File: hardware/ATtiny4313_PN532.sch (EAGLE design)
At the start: 22 parts, among them IC1 ATtiny4313, J2 AVR ISP, Q1 14.7456MHz, U1 PCA9543AD,118, U3 LTC490CN8PBF, U4 LTC490CN8PBF

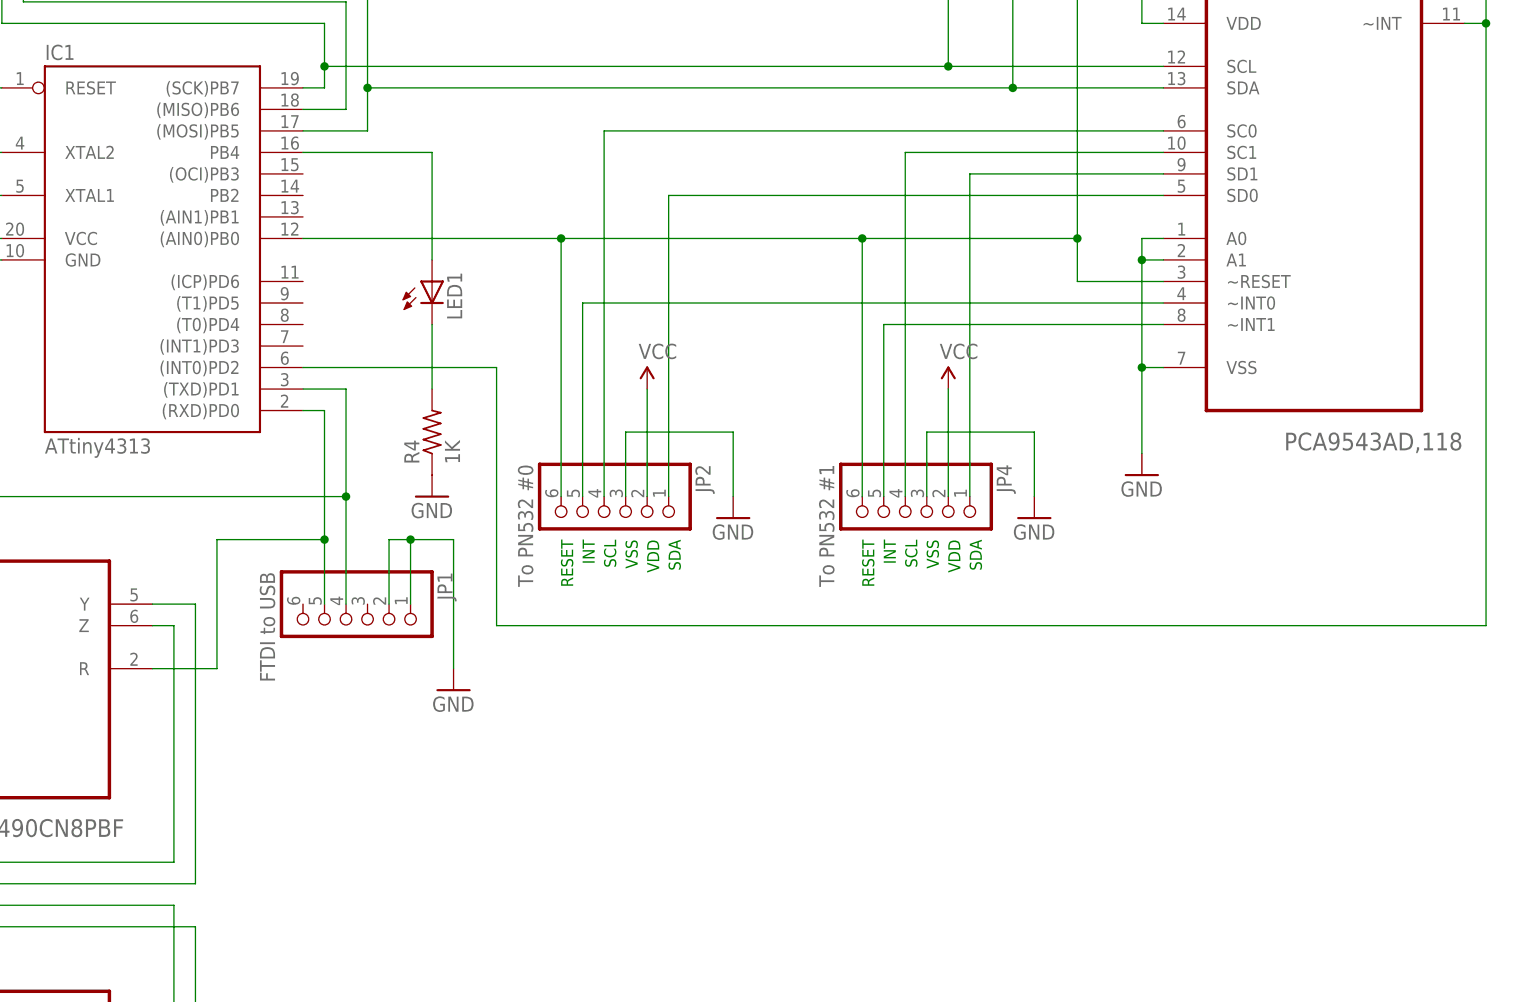
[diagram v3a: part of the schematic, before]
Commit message: Corrected wiring to LED and cleaned up a bit
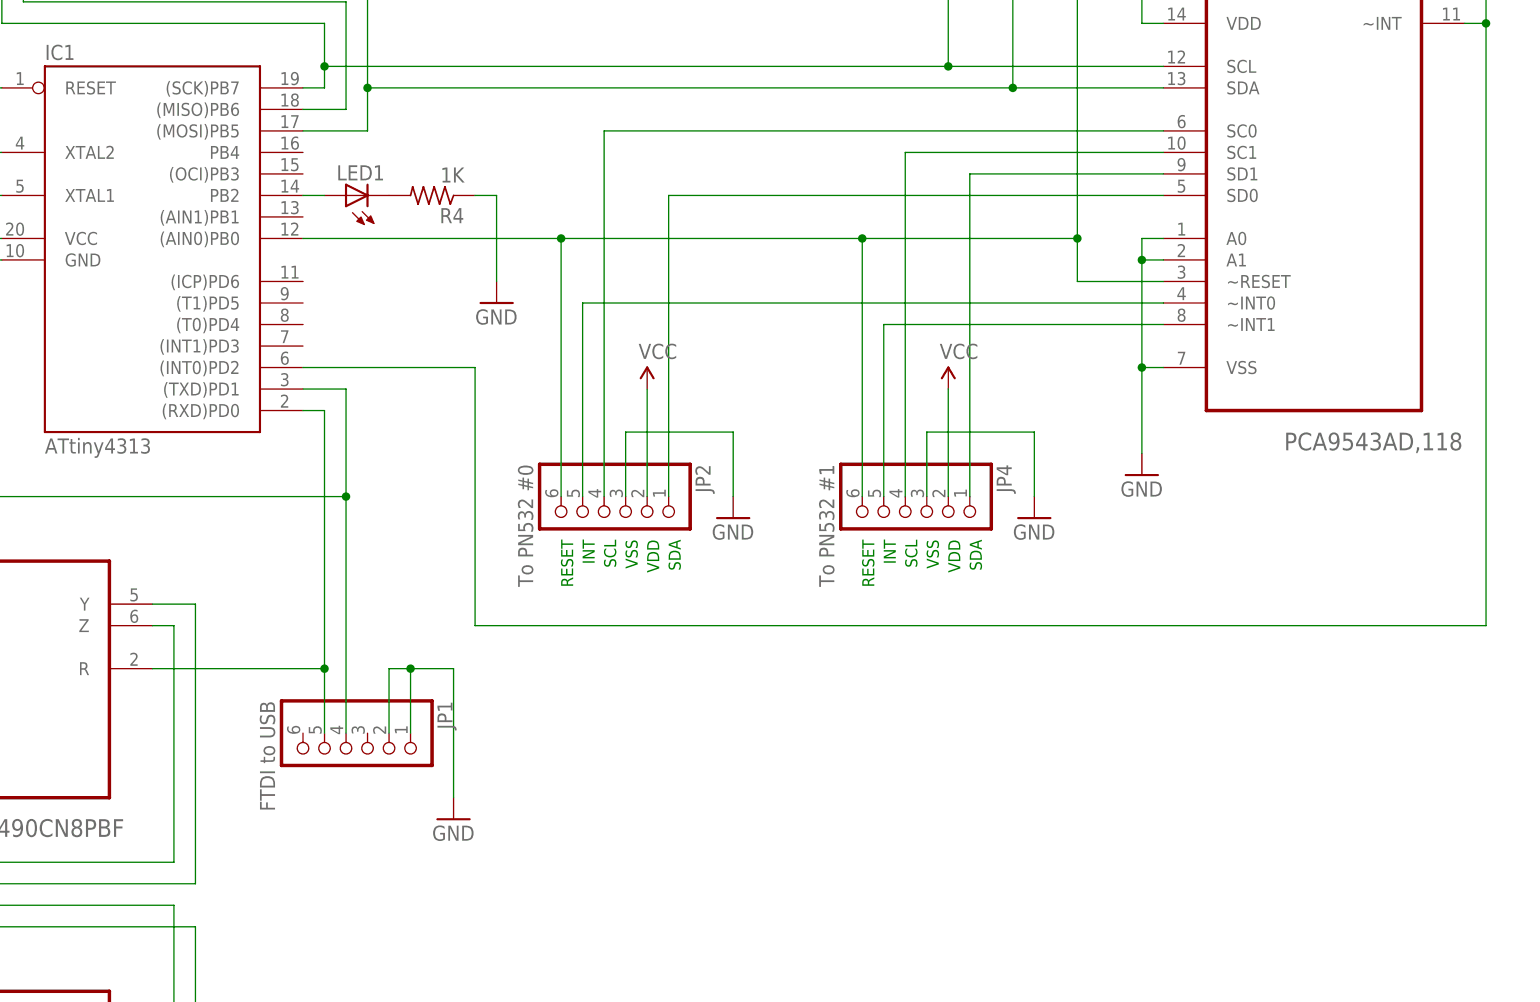
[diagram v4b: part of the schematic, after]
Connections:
- net N$9: now also IC1.PB2; no longer IC1.PB4
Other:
- moved on the sheet: JP1, LED1, R4
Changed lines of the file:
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@@
 <instance part="P+2" gate="1" x="203.2" y="175.26"/>
 <instance part="J2" gate="G$1" x="86.36" y="167.64"/>
-<instance part="JP1" gate="A" x="109.22" y="81.28" rot="R270"/>
-<instance part="GND3" gate="1" x="121.92" y="73.66"/>
-<instance part="LED1" gate="G$1" x="119.38" y="121.92"/>
-<instance part="R4" gate="G$1" x="119.38" y="104.14" rot="R90"/>
+<instance part="JP1" gate="A" x="109.22" y="66.04" rot="R270"/>
+<instance part="GND3" gate="1" x="121.92" y="58.42"/>
+<instance part="LED1" gate="G$1" x="109.22" y="132.08" rot="R90"/>
+<instance part="R4" gate="G$1" x="119.38" y="132.08" rot="R180"/>
 <instance part="P+3" gate="1" x="104.14" y="175.26"/>
-<instance part="GND4" gate="1" x="119.38" y="96.52"/>
+<instance part="GND4" gate="1" x="127" y="119.38"/>
 <instance part="GND5" gate="1" x="99.06" y="160.02"/>
 <instance part="JP2" gate="A" x="139.7" y="93.98" rot="R270"/>
@@
 <segment>
 <pinref part="GND3" gate="1" pin="GND"/>
-<wire x1="121.92" y1="91.44" x2="121.92" y2="76.2" width="0.1524" layer="91"/>
+<wire x1="121.92" y1="76.2" x2="121.92" y2="60.96" width="0.1524" layer="91"/>
 <pinref part="JP1" gate="A" pin="2"/>
-<wire x1="114.3" y1="83.82" x2="114.3" y2="91.44" width="0.1524" layer="91"/>
-<wire x1="114.3" y1="91.44" x2="116.84" y2="91.44" width="0.1524" layer="91"/>
+<wire x1="114.3" y1="68.58" x2="114.3" y2="76.2" width="0.1524" layer="91"/>
+<wire x1="114.3" y1="76.2" x2="116.84" y2="76.2" width="0.1524" layer="91"/>
 <pinref part="JP1" gate="A" pin="1"/>
-<wire x1="116.84" y1="91.44" x2="121.92" y2="91.44" width="0.1524" layer="91"/>
-<wire x1="116.84" y1="83.82" x2="116.84" y2="91.44" width="0.1524" layer="91"/>
-<junction x="116.84" y="91.44"/>
+<wire x1="116.84" y1="76.2" x2="121.92" y2="76.2" width="0.1524" layer="91"/>
+<wire x1="116.84" y1="68.58" x2="116.84" y2="76.2" width="0.1524" layer="91"/>
+<junction x="116.84" y="76.2"/>
 </segment>
 <segment>
 <pinref part="GND4" gate="1" pin="GND"/>
 <pinref part="R4" gate="G$1" pin="1"/>
+<wire x1="124.46" y1="132.08" x2="127" y2="132.08" width="0.1524" layer="91"/>
+<wire x1="127" y1="132.08" x2="127" y2="121.92" width="0.1524" layer="91"/>
 </segment>
 <segment>
@@
 <wire x1="45.72" y1="96.52" x2="109.22" y2="96.52" width="0.1524" layer="91"/>
 <pinref part="JP1" gate="A" pin="4"/>
-<wire x1="109.22" y1="96.52" x2="109.22" y2="83.82" width="0.1524" layer="91"/>
+<wire x1="109.22" y1="96.52" x2="109.22" y2="68.58" width="0.1524" layer="91"/>
 <junction x="109.22" y="96.52"/>
 </segment>
@@
 <pinref part="IC1" gate="G$1" pin="(RXD)PD0"/>
 <wire x1="104.14" y1="106.68" x2="106.68" y2="106.68" width="0.1524" layer="91"/>
-<wire x1="106.68" y1="106.68" x2="106.68" y2="91.44" width="0.1524" layer="91"/>
+<wire x1="106.68" y1="106.68" x2="106.68" y2="76.2" width="0.1524" layer="91"/>
 <pinref part="U3" gate="A" pin="R"/>
-<wire x1="86.36" y1="76.2" x2="93.98" y2="76.2" width="0.1524" layer="91"/>
-<wire x1="93.98" y1="76.2" x2="93.98" y2="91.44" width="0.1524" layer="91"/>
-<wire x1="93.98" y1="91.44" x2="106.68" y2="91.44" width="0.1524" layer="91"/>
+<wire x1="86.36" y1="76.2" x2="106.68" y2="76.2" width="0.1524" layer="91"/>
 <pinref part="JP1" gate="A" pin="5"/>
-<wire x1="106.68" y1="91.44" x2="106.68" y2="83.82" width="0.1524" layer="91"/>
-<junction x="106.68" y="91.44"/>
-</segment>
-</net>
-<net name="N$7" class="0">
-<segment>
-<pinref part="LED1" gate="G$1" pin="C"/>
-<pinref part="R4" gate="G$1" pin="2"/>
-<wire x1="119.38" y1="109.22" x2="119.38" y2="116.84" width="0.1524" layer="91"/>
-</segment>
-</net>
-<net name="N$9" class="0">
-<segment>
-<pinref part="IC1" gate="G$1" pin="PB4"/>
-<pinref part="LED1" gate="G$1" pin="A"/>
-<wire x1="104.14" y1="137.16" x2="119.38" y2="137.16" width="0.1524" layer="91"/>
-<wire x1="119.38" y1="137.16" x2="119.38" y2="124.46" width="0.1524" layer="91"/>
+<wire x1="106.68" y1="76.2" x2="106.68" y2="68.58" width="0.1524" layer="91"/>
+<junction x="106.68" y="76.2"/>
 </segment>
 </net>
@@
 <wire x1="243.84" y1="152.4" x2="243.84" y2="81.28" width="0.1524" layer="91"/>
 <junction x="243.84" y="152.4"/>
-<wire x1="243.84" y1="81.28" x2="127" y2="81.28" width="0.1524" layer="91"/>
-<wire x1="127" y1="81.28" x2="127" y2="111.76" width="0.1524" layer="91"/>
+<wire x1="243.84" y1="81.28" x2="124.46" y2="81.28" width="0.1524" layer="91"/>
+<wire x1="124.46" y1="81.28" x2="124.46" y2="111.76" width="0.1524" layer="91"/>
 <pinref part="IC1" gate="G$1" pin="(INT0)PD2"/>
-<wire x1="127" y1="111.76" x2="104.14" y2="111.76" width="0.1524" layer="91"/>
+<wire x1="124.46" y1="111.76" x2="104.14" y2="111.76" width="0.1524" layer="91"/>
 </segment>
 </net>
@@
 </segment>
 </net>
+<net name="N$7" class="0">
+<segment>
+<pinref part="LED1" gate="G$1" pin="C"/>
+<pinref part="R4" gate="G$1" pin="2"/>
+</segment>
+</net>
+<net name="N$9" class="0">
+<segment>
+<pinref part="IC1" gate="G$1" pin="PB2"/>
+<pinref part="LED1" gate="G$1" pin="A"/>
+<wire x1="104.14" y1="132.08" x2="106.68" y2="132.08" width="0.1524" layer="91"/>
+</segment>
+</net>
